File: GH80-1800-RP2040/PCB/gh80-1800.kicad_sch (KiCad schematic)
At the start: 278 parts, among them J1 USB_mini_micro_B, J2 ISP, J3 USB Header, J4 USB_mini_micro_B, J5 USB_mini_micro_B, K1 KEYSW, K10 KEYSW, K100 KEYSW, K101 KEYSW, K102 KEYSW, K103 KEYSW, K104 KEYSW, K105 KEYSW, K107 KEYSW, K108 KEYSW, K109 KEYSW, K11 KEYSW, K110 KEYSW, K12 KEYSW, K13 KEYSW, K14 KEYSW, K15 KEYSW, K16 KEYSW, K17 KEYSW, K18 KEYSW, K18-1 KEYSW, K19 KEYSW, K2 KEYSW, K20 KEYSW, K21 KEYSW, K22 KEYSW, K23 KEYSW, K24 KEYSW, K25 KEYSW, K26 KEYSW, K27 KEYSW, K28 KEYSW, K29 KEYSW, K3 KEYSW, K30 KEYSW, K31 KEYSW, K32 KEYSW, K33 KEYSW, K34 KEYSW, K35 KEYSW, K36 KEYSW, K37 KEYSW, K38 KEYSW, K39 KEYSW, K4 KEYSW, K40 KEYSW, K41 KEYSW, K42 KEYSW, K43 KEYSW, K44 KEYSW, K45 KEYSW, K46 KEYSW, K47 KEYSW, K48 KEYSW, K49 KEYSW, K5 KEYSW, K50 KEYSW, K51 KEYSW, K52 KEYSW, K53 KEYSW, K54 KEYSW, K55 KEYSW, K55-1 KEYSW, K56 KEYSW, K57 KEYSW, K58 KEYSW, K59 KEYSW, K6 KEYSW, K60 KEYSW, K61 KEYSW, K62 KEYSW, K63 KEYSW, K64 KEYSW, K65 KEYSW, K66 KEYSW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

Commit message: +1 to last commit, for got to save schematic change
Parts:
- removed R10: 1 0402, Resistor_SMD:R_0402_1005Metric, symbol Device:R_Small
- removed R9: 200 0603, Resistor_SMD:R_0603_1608Metric, symbol Device:R_Small
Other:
- note removed: "MAKE SURE THIS LINE is ran off of pin43 or close to pin43"
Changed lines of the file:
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@@
   (junction (at 254.635 484.505) (diameter 0) (color 0 0 0 0)
   )
-  (junction (at 290.83 44.45) (diameter 0) (color 0 0 0 0)
-  )
   (junction (at 234.95 60.96) (diameter 0) (color 0 0 0 0)
   )
@@
   (junction (at 104.775 357.505) (diameter 0) (color 0 0 0 0)
   )
-  (junction (at 290.83 60.96) (diameter 0) (color 0 0 0 0)
-  )
   (junction (at 142.875 438.785) (diameter 0) (color 0 0 0 0)
   )
@@
     (stroke (width 0) (type default) (color 0 0 0 0))
   )
-  (wire (pts (xy 290.83 33.02) (xy 290.83 35.56))
-    (stroke (width 0) (type default) (color 0 0 0 0))
-  )
   (wire (pts (xy 247.015 339.725) (xy 247.015 332.105))
     (stroke (width 0) (type default) (color 0 0 0 0))
@@
     (stroke (width 0) (type default) (color 0 0 0 0))
   )
-  (wire (pts (xy 289.56 60.96) (xy 290.83 60.96))
-    (stroke (width 0) (type default) (color 0 0 0 0))
-  )
   (wire (pts (xy 207.01 81.28) (xy 210.82 81.28))
     (stroke (width 0) (type default) (color 0 0 0 0))
@@
     (stroke (width 0) (type default) (color 0 0 0 0))
   )
-  (wire (pts (xy 290.83 44.45) (xy 298.45 44.45))
-    (stroke (width 0) (type default) (color 0 0 0 0))
-  )
   (wire (pts (xy 219.075 413.385) (xy 219.075 431.165))
     (stroke (width 0) (type default) (color 0 0 0 0))
@@
     (stroke (width 0) (type default) (color 0 0 0 0))
   )
-  (wire (pts (xy 290.83 60.96) (xy 290.83 52.07))
-    (stroke (width 0) (type default) (color 0 0 0 0))
-  )
   (wire (pts (xy 298.45 73.66) (xy 298.45 72.39))
     (stroke (width 0) (type default) (color 0 0 0 0))
@@
     (stroke (width 0) (type default) (color 0 0 0 0))
   )
-  (wire (pts (xy 290.83 60.96) (xy 298.45 60.96))
+  (wire (pts (xy 289.56 60.96) (xy 298.45 60.96))
     (stroke (width 0) (type default) (color 0 0 0 0))
   )
@@
     (stroke (width 0) (type default) (color 0 0 0 0))
   )
-  (wire (pts (xy 290.83 40.64) (xy 290.83 44.45))
-    (stroke (width 0) (type default) (color 0 0 0 0))
-  )
   (wire (pts (xy 48.006 59.436) (xy 48.006 61.976))
     (stroke (width 0) (type default) (color 0 0 0 0))
@@
     (stroke (width 0) (type default) (color 0 0 0 0))
   )
-  (wire (pts (xy 290.83 44.45) (xy 290.83 46.99))
-    (stroke (width 0) (type default) (color 0 0 0 0))
-  )
   (wire (pts (xy 104.775 431.165) (xy 104.775 454.025))
     (stroke (width 0) (type default) (color 0 0 0 0))
@@
     (effects (font (size 1.27 1.27)) (justify left bottom))
   )
-  (text "MAKE SURE THIS LINE is ran off of pin43\nor close to pin43"
-    (at 248.92 41.91 0)
-    (effects (font (size 1.27 1.27)) (justify left bottom))
-  )
   (text "Reset button" (at 131.064 154.94 0)
     (effects (font (size 1.27 1.27) bold) (justify left bottom))
@@
     (effects (font (size 1.27 1.27)) (justify left bottom))
   )
-  (label "ADC_VREF" (at 298.45 44.45 0)
-    (effects (font (size 1.27 1.27)) (justify left bottom))
-  )
   (label "QSPI_SD2" (at 53.34 138.43 0)
     (effects (font (size 1.27 1.27)) (justify left bottom))
@@
     (pin "1")
   )
-  (symbol (lib_id "Device:R_Small") (at 290.83 49.53 0) (unit 1)
-    (in_bom yes) (on_board yes)
-    (property "Reference" "R10" (id 0) (at 292.3286 48.3616 0)
-      (effects (font (size 1.27 1.27)) (justify left))
-    )
-    (property "Value" "1 0402" (id 1) (at 292.3286 50.673 0)
-      (effects (font (size 1.27 1.27)) (justify left))
-    )
-    (property "Footprint" "Resistor_SMD:R_0402_1005Metric" (id 2) (at 290.83 49.53 0)
-      (effects (font (size 1.27 1.27)) hide)
-    )
-    (property "Datasheet" "" (id 3) (at 290.83 49.53 0)
-      (effects (font (size 1.27 1.27)) hide)
-    )
-    (property "LCSC" " " (id 4) (at 290.83 49.53 0)
-      (effects (font (size 1.27 1.27)) hide)
-    )
-    (pin "1")
-    (pin "2")
-  )
-  (symbol (lib_id "Device:R_Small") (at 290.83 38.1 0) (unit 1)
-    (in_bom yes) (on_board yes)
-    (property "Reference" "R9" (id 0) (at 292.3286 36.9316 0)
-      (effects (font (size 1.27 1.27)) (justify left))
-    )
-    (property "Value" "200 0603" (id 1) (at 292.3286 39.243 0)
-      (effects (font (size 1.27 1.27)) (justify left))
-    )
-    (property "Footprint" "Resistor_SMD:R_0603_1608Metric" (id 2) (at 290.83 38.1 0)
-      (effects (font (size 1.27 1.27)) hide)
-    )
-    (property "Datasheet" "" (id 3) (at 290.83 38.1 0)
-      (effects (font (size 1.27 1.27)) hide)
-    )
-    (property "LCSC" " " (id 4) (at 290.83 38.1 0)
-      (effects (font (size 1.27 1.27)) hide)
-    )
-    (pin "1")
-    (pin "2")
-  )
-  (symbol (lib_id "power:+3.3V") (at 290.83 33.02 0) (unit 1)
-    (in_bom yes) (on_board yes)
-    (property "Reference" "#PWR013" (id 0) (at 290.83 36.83 0)
-      (effects (font (size 1.27 1.27)) hide)
-    )
-    (property "Value" "+3.3V" (id 1) (at 291.211 28.6258 0))
-    (property "Footprint" "" (id 2) (at 290.83 33.02 0)
-      (effects (font (size 1.27 1.27)) hide)
-    )
-    (property "Datasheet" "" (id 3) (at 290.83 33.02 0)
-      (effects (font (size 1.27 1.27)) hide)
-    )
-    (pin "1")
-  )
   (symbol (lib_id "Device:D_Schottky") (at 62.23 44.45 180) (unit 1)
     (in_bom yes) (on_board yes)
@@
       (reference "#PWR011") (unit 1) (value "VCC") (footprint "")
     )
-    (path "/00000000-0000-0000-0000-000061045079"
-      (reference "#PWR013") (unit 1) (value "+3.3V") (footprint "")
-    )
     (path "/00000000-0000-0000-0000-00005edc8ac7"
       (reference "#PWR015") (unit 1) (value "GND") (footprint "")
@@
       (reference "R4") (unit 1) (value "27 0402 Resistor") (footprint "Resistor_SMD:R_0402_1005Metric")
     )
-    (path "/00000000-0000-0000-0000-000061044b24"
-      (reference "R9") (unit 1) (value "200 0603") (footprint "Resistor_SMD:R_0603_1608Metric")
-    )
-    (path "/00000000-0000-0000-0000-0000610441d8"
-      (reference "R10") (unit 1) (value "1 0402") (footprint "Resistor_SMD:R_0402_1005Metric")
-    )
     (path "/00000000-0000-0000-0000-00006150e6ab"

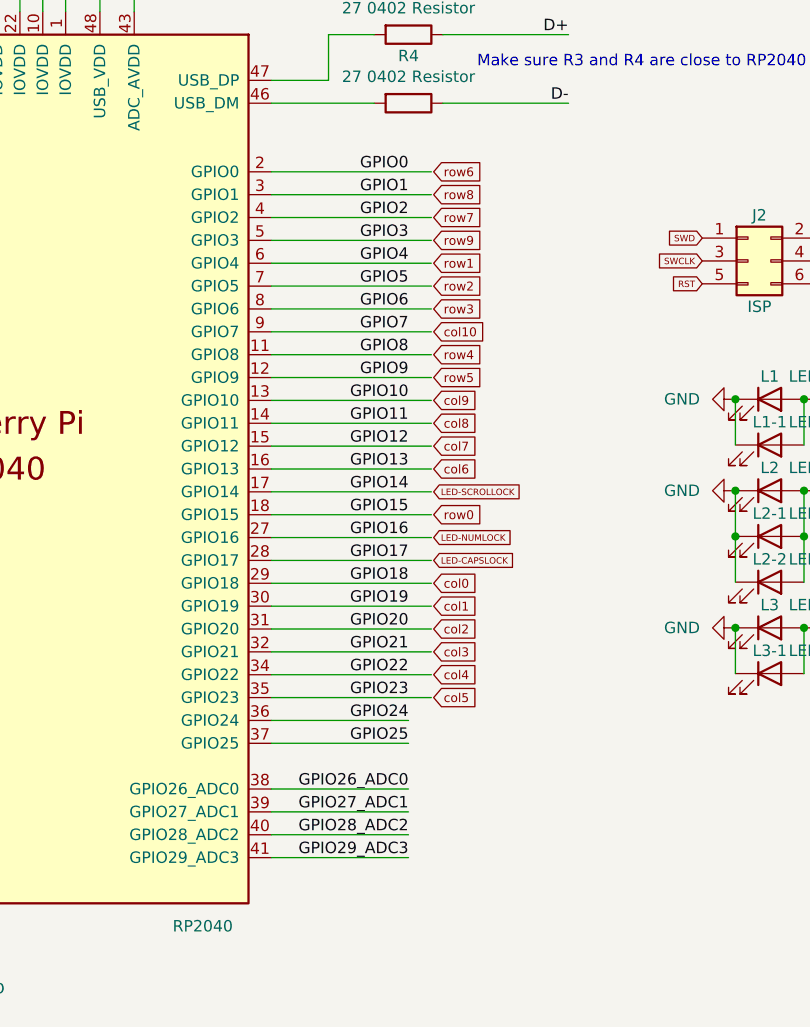
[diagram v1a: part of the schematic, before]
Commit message: Finished col/row traces.
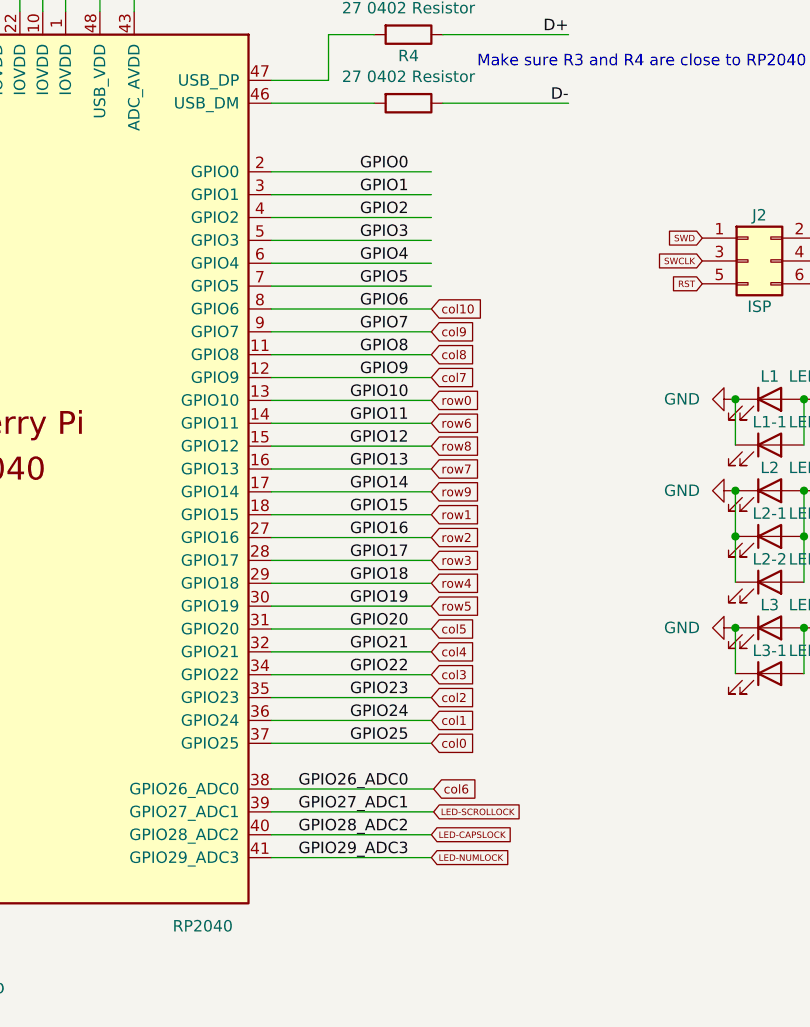
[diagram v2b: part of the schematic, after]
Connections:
- net GPIO10 is gone; now on net row0: U3.13 (GPIO10)
- net GPIO11 is gone; now on net row6: U3.14 (GPIO11)
- net GPIO12 is gone; now on net row8: U3.15 (GPIO12)
- net GPIO13 is gone; now on net row7: U3.16 (GPIO13)
- net GPIO14 is gone; now on net row9: U3.17 (GPIO14)
- net GPIO15 is gone; now on net row1: U3.18 (GPIO15)
- net GPIO16 is gone; now on net row2: U3.27 (GPIO16)
- net GPIO17 is gone; now on net row3: U3.28 (GPIO17)
- net GPIO18 is gone; now on net row4: U3.29 (GPIO18)
- net GPIO19 is gone; now on net row5: U3.30 (GPIO19)
- net GPIO20 is gone; now on net col5: U3.31 (GPIO20)
- net GPIO21 is gone; now on net col4: U3.32 (GPIO21)
- net GPIO22 is gone; now on net col3: U3.34 (GPIO22)
- net GPIO23 is gone; now on net col2: U3.35 (GPIO23)
- net GPIO24 is gone; now on net col1: U3.36 (GPIO24)
- net GPIO25 is gone; now on net col0: U3.37 (GPIO25)
- net GPIO26_ADC0 is gone; now on net col6: U3.38 (GPIO26_ADC0)
- net GPIO27_ADC1 is gone; now on net LED-SCROLLOCK: U3.39 (GPIO27_ADC1)
- net GPIO28_ADC2 is gone; now on net LED-CAPSLOCK: U3.40 (GPIO28_ADC2)
- net GPIO29_ADC3 is gone; now on net LED-NUMLOCK: U3.41 (GPIO29_ADC3)
- net GPIO6 is gone; now on net col10: U3.8 (GPIO6)
- net GPIO7 is gone; now on net col9: U3.9 (GPIO7)
- net GPIO8 is gone; now on net col8: U3.11 (GPIO8)
- net GPIO9 is gone; now on net col7: U3.12 (GPIO9)

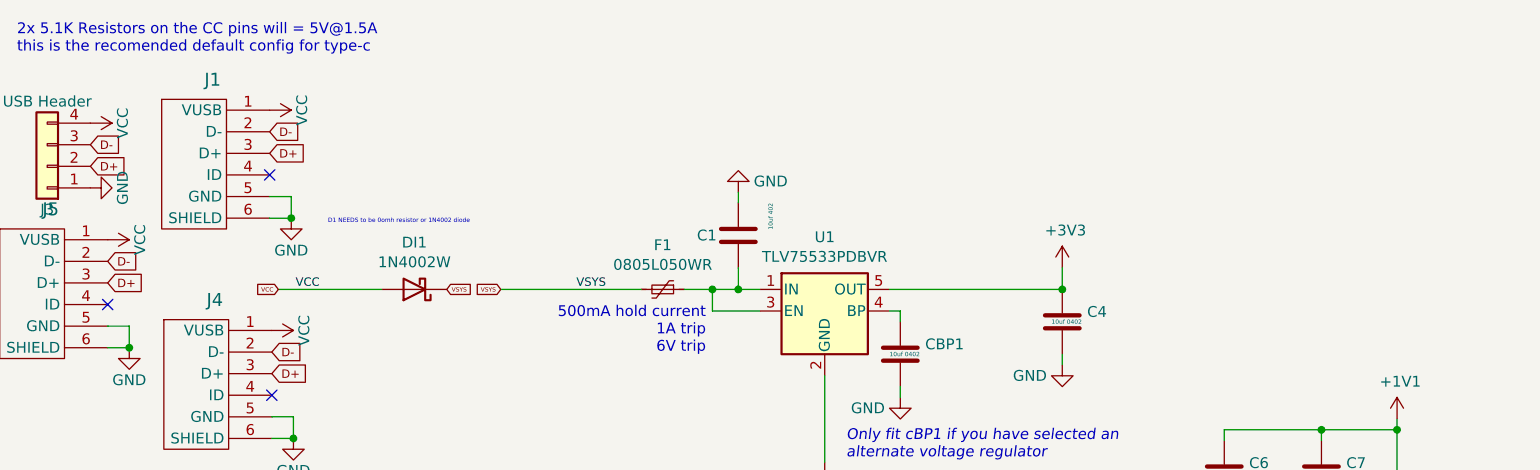
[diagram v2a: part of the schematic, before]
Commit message: replaced type-b port with type-c and generated gerber and CPL
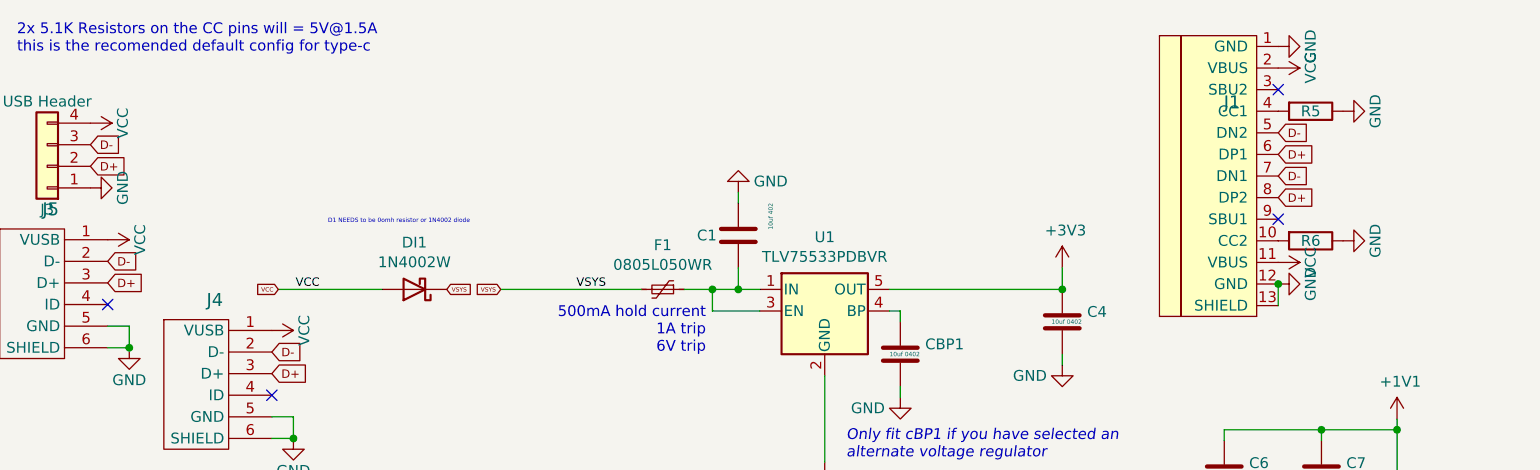
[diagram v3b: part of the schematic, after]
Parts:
- added R5, R6: 5.1K 0402 Resistor, Resistor_SMD:R_0402_1005Metric, symbol Device:R
- J1: footprint Keeb_components:USB_Mini_SMD -> Type-C:HRO-TYPE-C-31-M-12; symbol keyboard_parts:USB_mini_micro_B -> Type-C:HRO-TYPE-C-31-M-12
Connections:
- net D+: now also J1.6 (DP1), J1.8 (DP2); no longer J1.3 (D+)
- net D-: now also J1.5 (DN2), J1.7 (DN1); no longer J1.2 (D-)
- net GND: now also J1.1 (GND), J1.12 (GND), J1.13 (SHIELD), R5.1, R6.1; no longer J1.5 (GND), J1.6 (SHIELD)
- net VCC: now also J1.11 (VBUS), J1.2 (VBUS); no longer J1.1 (VUSB)
- net at J1.4 (CC1): now also R5.2
- new net: J1.10 (CC2), R6.2
- no-connect marks 3 -> 4
